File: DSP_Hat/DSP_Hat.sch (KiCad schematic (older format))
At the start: 27 parts, among them P1 Conn_02x20_Odd_Even

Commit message: more work on timing crytal
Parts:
- added C?: 0.1uF, symbol Device:C_Small
- added L?: L_Core_Ferrite, symbol Device:L_Core_Ferrite
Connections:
- wire segments 129 -> 139
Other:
- moved on the sheet: R?
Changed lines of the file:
@@
 U 1 1 5CABFE49
 P 10000 2900
-F 0 "X?" H 10000 2422 50  0000 C CNN
-F 1 "25MHz" H 10000 2513 50  0000 C CNN
+F 0 "X?" H 10250 2500 50  0000 R CNN
+F 1 "25MHz" H 10300 2600 50  0000 R CNN
 F 2 "Oscillator:Oscillator_SMD_Abracon_ASV-4Pin_7.0x5.1mm" H 10700 2550 50  0001 C CNN
 F 3 "http://www.abracon.com/Oscillators/ASV.pdf" H 9900 2900 50  0001 C CNN
@@
 Text Label 9000 2900 2    50   ~ 0
 MCLK
-Wire Wire Line
-	10000 3200 10000 3450
-Wire Wire Line
-	10000 3450 10600 3450
 $Comp
 L power:GND #PWR?
 U 1 1 5CADBC01
-P 10600 3450
-F 0 "#PWR?" H 10600 3200 50  0001 C CNN
-F 1 "GND" V 10605 3322 50  0000 R CNN
-F 2 "" H 10600 3450 50  0001 C CNN
-F 3 "" H 10600 3450 50  0001 C CNN
-	1    10600 3450
+P 10600 2400
+F 0 "#PWR?" H 10600 2150 50  0001 C CNN
+F 1 "GND" V 10605 2272 50  0000 R CNN
+F 2 "" H 10600 2400 50  0001 C CNN
+F 3 "" H 10600 2400 50  0001 C CNN
+	1    10600 2400
 	0    -1   -1   0
 $EndComp
@@
 L Device:R R?
 U 1 1 5CAE0FF9
-P 10500 2900
-F 0 "R?" V 10293 2900 50  0000 C CNN
-F 1 "10k" V 10384 2900 50  0000 C CNN
-F 2 "" V 10430 2900 50  0001 C CNN
-F 3 "~" H 10500 2900 50  0001 C CNN
-	1    10500 2900
+P 10600 2900
+F 0 "R?" V 10715 2900 50  0000 C CNN
+F 1 "10k" V 10806 2900 50  0000 C CNN
+F 2 "" V 10530 2900 50  0001 C CNN
+F 3 "~" H 10600 2900 50  0001 C CNN
+	1    10600 2900
+	0    1    1    0
+$EndComp
+Wire Wire Line
+	10750 2900 10800 2900
+Wire Wire Line
+	10300 2900 10450 2900
+Wire Wire Line
+	10000 2600 10000 2400
+Wire Wire Line
+	10000 2400 10350 2400
+Wire Wire Line
+	10000 3450 10250 3450
+$Comp
+L Device:L_Core_Ferrite L?
+U 1 1 5CA3E2B6
+P 10400 3450
+F 0 "L?" V 10532 3450 50  0000 C CNN
+F 1 "L_Core_Ferrite" V 10623 3450 50  0000 C CNN
+F 2 "" H 10400 3450 50  0001 C CNN
+F 3 "~" H 10400 3450 50  0001 C CNN
+	1    10400 3450
 	0    1    1    0
 $EndComp
 $Comp
-L power:GND #PWR?
-U 1 1 5CAE5CF4
-P 10800 2900
-F 0 "#PWR?" H 10800 2650 50  0001 C CNN
-F 1 "GND" V 10805 2772 50  0000 R CNN
-F 2 "" H 10800 2900 50  0001 C CNN
-F 3 "" H 10800 2900 50  0001 C CNN
-	1    10800 2900
-	0    -1   -1   0
+L power:+3.3V #PWR?
+U 1 1 5CA449F1
+P 10650 3450
+F 0 "#PWR?" H 10650 3300 50  0001 C CNN
+F 1 "+3.3V" V 10665 3578 50  0000 L CNN
+F 2 "" H 10650 3450 50  0001 C CNN
+F 3 "" H 10650 3450 50  0001 C CNN
+	1    10650 3450
+	0    1    1    0
 $EndComp
 Wire Wire Line
-	10650 2900 10800 2900
+	10550 3450 10650 3450
 Wire Wire Line
-	10300 2900 10350 2900
+	10000 3200 10000 3250
+$Comp
+L Device:C_Small C?
+U 1 1 5CA6F896
+P 10350 2650
+F 0 "C?" H 10442 2696 50  0000 L CNN
+F 1 "0.1uF" H 10442 2605 50  0000 L CNN
+F 2 "" H 10350 2650 50  0001 C CNN
+F 3 "~" H 10350 2650 50  0001 C CNN
+	1    10350 2650
+	1    0    0    -1
+$EndComp
+Wire Wire Line
+	10350 2550 10350 2400
+Connection ~ 10350 2400
+Wire Wire Line
+	10350 2400 10600 2400
+Wire Wire Line
+	10800 2900 10800 3250
+Wire Wire Line
+	10800 3250 10000 3250
+Connection ~ 10000 3250
+Wire Wire Line
+	10000 3250 10000 3450
+Wire Wire Line
+	10350 2750 10350 3200
+Wire Wire Line
+	10350 3200 10000 3200
+Connection ~ 10000 3200
 $EndSCHEMATC

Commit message: more work on schematic
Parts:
- removed R?: 49.9, symbol Device:R
- removed Y?: 25 MHz, symbol Device:Crystal
- gave numbers to parts that had none: 22
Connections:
- wire segments 139 -> 137

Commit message: farted around some more with DSP Hat
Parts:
- R2, R3, R4, R5: footprint (none) -> Resistor_SMD:R_0402_1005Metric
- U1: footprint CP_32_4 -> DSP_Hat:ADAU1761BCPZ-R7
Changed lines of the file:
@@
 F 0 "U1" H 5750 4587 60  0000 C CNN
 F 1 "ADAU1761BCPZ-R7" H 5750 4481 60  0000 C CNN
-F 2 "CP_32_4" H 5750 4440 60  0001 C CNN
+F 2 "DSP_Hat:ADAU1761BCPZ-R7" H 5750 4440 60  0001 C CNN
 F 3 "" H 3650 4200 60  0000 C CNN
 	1    3650 4200
@@
 F 0 "R2" H 6670 2096 50  0000 L CNN
 F 1 "2k" H 6670 2005 50  0000 L CNN
-F 2 "" V 6530 2050 50  0001 C CNN
+F 2 "Resistor_SMD:R_0402_1005Metric" V 6530 2050 50  0001 C CNN
 F 3 "~" H 6600 2050 50  0001 C CNN
 	1    6600 2050
@@
 F 0 "R3" H 6670 2496 50  0000 L CNN
 F 1 "2k" H 6670 2405 50  0000 L CNN
-F 2 "" V 6530 2450 50  0001 C CNN
+F 2 "Resistor_SMD:R_0402_1005Metric" V 6530 2450 50  0001 C CNN
 F 3 "~" H 6600 2450 50  0001 C CNN
 	1    6600 2450
@@
 F 0 "R4" V 9193 2900 50  0000 C CNN
 F 1 "49.9" V 9284 2900 50  0000 C CNN
-F 2 "" V 9330 2900 50  0001 C CNN
+F 2 "Resistor_SMD:R_0402_1005Metric" V 9330 2900 50  0001 C CNN
 F 3 "~" H 9400 2900 50  0001 C CNN
 	1    9400 2900
@@
 F 0 "R5" V 10715 2900 50  0000 C CNN
 F 1 "10k" V 10806 2900 50  0000 C CNN
-F 2 "" V 10530 2900 50  0001 C CNN
+F 2 "Resistor_SMD:R_0402_1005Metric" V 10530 2900 50  0001 C CNN
 F 3 "~" H 10600 2900 50  0001 C CNN
 	1    10600 2900

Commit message: placing more PCB footprints
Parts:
- added C13: 9.1 pF, Capacitor_SMD:C_0603_1608Metric_Pad1.05x0.95mm_HandSolder, symbol Device:C_Small
- C1, C2: footprint (none) -> Capacitor_SMD:C_0805_2012Metric_Pad1.15x1.40mm_HandSolder
- C3, C4, C5: footprint (none) -> Capacitor_SMD:C_0603_1608Metric_Pad1.05x0.95mm_HandSolder
- L2: footprint (none) -> Inductor_SMD:L_0402_1005Metric
- R4: footprint Resistor_SMD:R_0402_1005Metric -> Resistor_SMD:R_0603_1608Metric
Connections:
- wire segments 137 -> 138
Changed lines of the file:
@@
 F 0 "C2" H 1688 4446 50  0000 L CNN
 F 1 "10uF" H 1688 4355 50  0000 L CNN
-F 2 "" H 1600 4400 50  0001 C CNN
+F 2 "Capacitor_SMD:C_0805_2012Metric_Pad1.15x1.40mm_HandSolder" H 1600 4400 50  0001 C CNN
 F 3 "~" H 1600 4400 50  0001 C CNN
 	1    1600 4400
@@
 F 0 "C4" H 2092 4446 50  0000 L CNN
 F 1 "0.1uF" H 2092 4355 50  0000 L CNN
-F 2 "" H 2000 4400 50  0001 C CNN
+F 2 "Capacitor_SMD:C_0603_1608Metric_Pad1.05x0.95mm_HandSolder" H 2000 4400 50  0001 C CNN
 F 3 "~" H 2000 4400 50  0001 C CNN
 	1    2000 4400
@@
 	0    -1   -1   0
 $EndComp
-Wire Wire Line
-	3650 4900 2300 4900
 $Comp
 L power:+3.3V #PWR01
@@
 L power:GND #PWR07
 U 1 1 5CA96405
-P 2650 5400
-F 0 "#PWR07" H 2650 5150 50  0001 C CNN
-F 1 "GND" V 2655 5272 50  0000 R CNN
-F 2 "" H 2650 5400 50  0001 C CNN
-F 3 "" H 2650 5400 50  0001 C CNN
-	1    2650 5400
+P 2650 5650
+F 0 "#PWR07" H 2650 5400 50  0001 C CNN
+F 1 "GND" V 2655 5522 50  0000 R CNN
+F 2 "" H 2650 5650 50  0001 C CNN
+F 3 "" H 2650 5650 50  0001 C CNN
+	1    2650 5650
 	0    -1   -1   0
 $EndComp
@@
 F 0 "C1" H 1238 5196 50  0000 L CNN
 F 1 "10uF" H 1238 5105 50  0000 L CNN
-F 2 "" H 1150 5150 50  0001 C CNN
+F 2 "Capacitor_SMD:C_0805_2012Metric_Pad1.15x1.40mm_HandSolder" H 1150 5150 50  0001 C CNN
 F 3 "~" H 1150 5150 50  0001 C CNN
 	1    1150 5150
@@
 F 0 "C3" H 1692 5196 50  0000 L CNN
 F 1 "0.1uF" H 1692 5105 50  0000 L CNN
-F 2 "" H 1600 5150 50  0001 C CNN
+F 2 "Capacitor_SMD:C_0603_1608Metric_Pad1.05x0.95mm_HandSolder" H 1600 5150 50  0001 C CNN
 F 3 "~" H 1600 5150 50  0001 C CNN
 	1    1600 5150
@@
 F 0 "C5" H 2142 5196 50  0000 L CNN
 F 1 "0.1uF" H 2142 5105 50  0000 L CNN
-F 2 "" H 2050 5150 50  0001 C CNN
+F 2 "Capacitor_SMD:C_0603_1608Metric_Pad1.05x0.95mm_HandSolder" H 2050 5150 50  0001 C CNN
 F 3 "~" H 2050 5150 50  0001 C CNN
 	1    2050 5150
 	-1   0    0    -1
 $EndComp
-$Comp
-L pspice:INDUCTOR L1
-U 1 1 5CA96686
-P 2300 5150
-F 0 "L1" V 2254 5228 50  0000 L CNN
-F 1 "1.2nH" V 2345 5228 50  0000 L CNN
-F 2 "" H 2300 5150 50  0001 C CNN
-F 3 "~" H 2300 5150 50  0001 C CNN
-	1    2300 5150
-	0    1    1    0
-$EndComp
-Connection ~ 2300 4900
 Wire Wire Line
 	1150 4900 1150 5050
@@
 	2050 4900 2300 4900
 Wire Wire Line
-	1150 5250 1150 5400
-Wire Wire Line
-	1150 5400 1600 5400
-Connection ~ 2300 5400
-Wire Wire Line
-	2300 5400 2650 5400
-Wire Wire Line
-	1600 5250 1600 5400
-Connection ~ 1600 5400
-Wire Wire Line
-	1600 5400 2050 5400
-Wire Wire Line
-	2050 5250 2050 5400
-Connection ~ 2050 5400
-Wire Wire Line
-	2050 5400 2300 5400
+	1150 5250 1150 5650
+Wire Wire Line
+	1150 5650 1600 5650
+Wire Wire Line
+	2050 5250 2050 5650
 Wire Wire Line
 	3500 4300 3650 4300
@@
 F 0 "R4" V 9193 2900 50  0000 C CNN
 F 1 "49.9" V 9284 2900 50  0000 C CNN
-F 2 "Resistor_SMD:R_0402_1005Metric" V 9330 2900 50  0001 C CNN
+F 2 "Resistor_SMD:R_0603_1608Metric" V 9330 2900 50  0001 C CNN
 F 3 "~" H 9400 2900 50  0001 C CNN
 	1    9400 2900
@@
 F 0 "L2" V 10532 3450 50  0000 C CNN
 F 1 "L_Core_Ferrite" V 10623 3450 50  0000 C CNN
-F 2 "" H 10400 3450 50  0001 C CNN
+F 2 "Inductor_SMD:L_0402_1005Metric" H 10400 3450 50  0001 C CNN
 F 3 "~" H 10400 3450 50  0001 C CNN
 	1    10400 3450
@@
 Text Label 3500 4300 2    50   ~ 0
 MCLK
+$Comp
+L pspice:INDUCTOR L1
+U 1 1 5CA96686
+P 2300 5200
+F 0 "L1" V 2254 5278 50  0000 L CNN
+F 1 "1.2nH" V 2345 5278 50  0000 L CNN
+F 2 "" H 2300 5200 50  0001 C CNN
+F 3 "~" H 2300 5200 50  0001 C CNN
+	1    2300 5200
+	0    1    1    0
+$EndComp
+Connection ~ 2300 4900
+Wire Wire Line
+	2300 4900 3650 4900
+Wire Wire Line
+	2050 5650 2300 5650
+Connection ~ 2050 5650
+Wire Wire Line
+	1600 5250 1600 5650
+Connection ~ 1600 5650
+Wire Wire Line
+	1600 5650 2050 5650
+$Comp
+L Device:C_Small C13
+U 1 1 5CAE5AF1
+P 2300 5550
+F 0 "C13" H 2208 5596 50  0000 R CNN
+F 1 "9.1 pF" H 2208 5505 50  0000 R CNN
+F 2 "Capacitor_SMD:C_0603_1608Metric_Pad1.05x0.95mm_HandSolder" H 2300 5550 50  0001 C CNN
+F 3 "~" H 2300 5550 50  0001 C CNN
+	1    2300 5550
+	-1   0    0    -1
+$EndComp
+Connection ~ 2300 5650
+Wire Wire Line
+	2300 5650 2650 5650
+Wire Wire Line
+	2300 4950 2300 4900
 $EndSCHEMATC

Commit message: overhaul of schematic
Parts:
- removed C1, C2: 10uF, Capacitor_SMD:C_0805_2012Metric_Pad1.15x1.40mm_HandSolder, symbol Device:CP_Small
- removed C10, C11: 0.1uF, symbol Device:C_Small
- removed C12: 10uF, symbol Device:CP_Small
- removed C13: 9.1 pF, Capacitor_SMD:C_0603_1608Metric_Pad1.05x0.95mm_HandSolder, symbol Device:C_Small
- removed C3, C4, C5: 0.1uF, Capacitor_SMD:C_0603_1608Metric_Pad1.05x0.95mm_HandSolder, symbol Device:C_Small
- removed C6, C7, C8, C9: 10uf, symbol Device:C
- removed L1: 1.2nH, symbol pspice:INDUCTOR
- removed L2: L_Core_Ferrite, Inductor_SMD:L_0402_1005Metric, symbol Device:L_Core_Ferrite
- removed MK5: Left Microphone, symbol Device:Microphone
- removed MK6: Right Microphone, symbol Device:Microphone
- removed R2, R3: 2k, Resistor_SMD:R_0402_1005Metric, symbol Device:R
- removed R4: 49.9, Resistor_SMD:R_0603_1608Metric, symbol Device:R
- removed R5: 10k, Resistor_SMD:R_0402_1005Metric, symbol Device:R
- removed U1: ADAU1761BCPZ-R7, DSP_Hat:ADAU1761BCPZ-R7, symbol 2019-03-30_11-52-36:ADAU1761BCPZ-R7
- removed X1: 25MHz, Oscillator:Oscillator_SMD_Abracon_ASV-4Pin_7.0x5.1mm, symbol Oscillator:ASV-xxxMHz
- added C? (x11): CAP, symbol pspice:CAP
- added J?: AudioJack2_Ground_Switch, symbol Connector:AudioJack2_Ground_Switch
- added L?: L_Core_Ferrite, symbol Device:L_Core_Ferrite
- added R? (x6): R, symbol Device:R
- added U?: ADAU1761BCPZ-R7_2, CP_32_4, symbol 2019-03-30_11-52-36:ADAU1761BCPZ-R7_2
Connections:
- net labels added: ADAIU761_ADDR0, ADAIU761_ADDR1, ADC_SDATA, BCLK, DAC_SDATA, LEFT_LOOP, LOUTN, LOUTP, LRCLK, RIGHT_LOOP, ROUTN, ROUTP, TWI0_SCL, TWIO_SDA
- net labels removed: LINN, LINP, MCLK, MICBIAS, RINN, RINP
- wire segments 138 -> 145

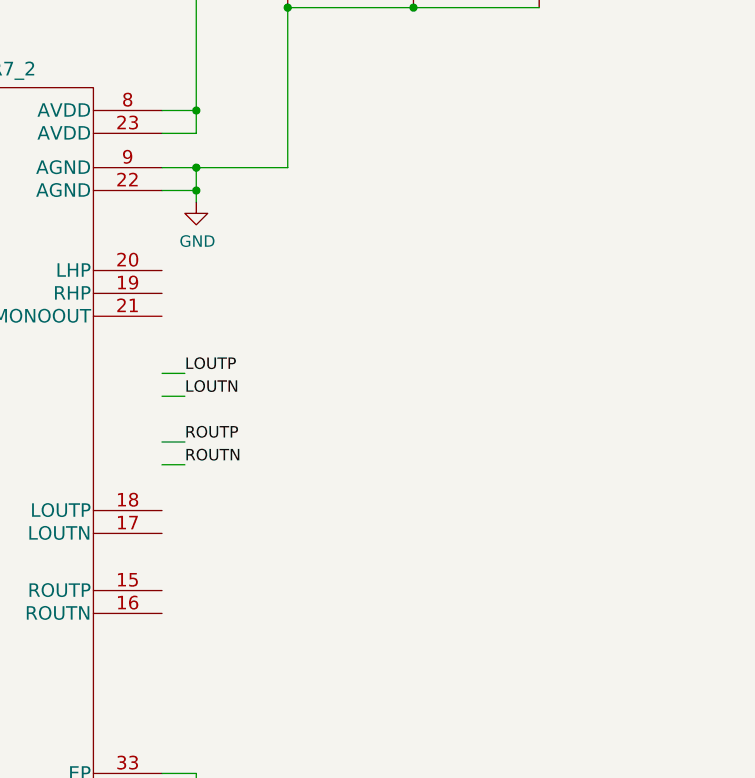
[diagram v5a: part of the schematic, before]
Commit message: edits to symbol for ADAU1761
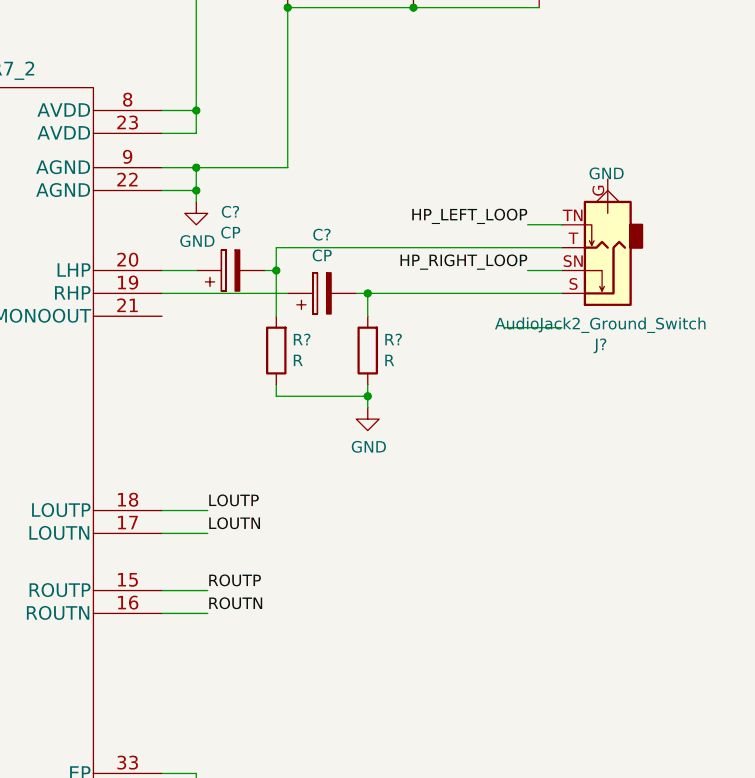
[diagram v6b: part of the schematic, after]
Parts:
- added C? (x2): CP, symbol Device:CP
- added J?: AudioJack2_Ground_Switch, symbol Connector:AudioJack2_Ground_Switch
- added R? (x2): R, symbol Device:R
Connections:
- net labels added: HP_LEFT_LOOP, HP_RIGHT_LOOP
- wire segments 145 -> 161
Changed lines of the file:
@@
 	6050 6500 6550 6500
 Connection ~ 6550 6500
-Wire Wire Line
-	8800 4050 8900 4050
-Wire Wire Line
-	8800 4150 8900 4150
-Wire Wire Line
-	8800 4350 8900 4350
-Wire Wire Line
-	8800 4450 8900 4450
-Text Label 8900 4050 0    50   ~ 0
-LOUTP
-Text Label 8900 4150 0    50   ~ 0
-LOUTN
-Text Label 8900 4350 0    50   ~ 0
-ROUTP
-Text Label 8900 4450 0    50   ~ 0
-ROUTN
 $Comp
 L power:GND #PWR?
@@
 	1    0    0    -1
 $EndComp
+$Comp
+L Connector:AudioJack2_Ground_Switch J?
+U 1 1 5CCA20D9
+P 10750 3500
+F 0 "J?" H 10780 3925 50  0000 C CNN
+F 1 "AudioJack2_Ground_Switch" H 10780 3834 50  0000 C CNN
+F 2 "" H 10750 3700 50  0001 C CNN
+F 3 "~" H 10750 3700 50  0001 C CNN
+	1    10750 3500
+	-1   0    0    1
+$EndComp
+$Comp
+L power:GND #PWR?
+U 1 1 5CCA2325
+P 10750 3350
+F 0 "#PWR?" H 10750 3100 50  0001 C CNN
+F 1 "GND" H 10755 3177 50  0000 C CNN
+F 2 "" H 10750 3350 50  0001 C CNN
+F 3 "" H 10750 3350 50  0001 C CNN
+	1    10750 3350
+	-1   0    0    1
+$EndComp
+$Comp
+L Device:CP C?
+U 1 1 5CCA2D40
+P 9100 3600
+F 0 "C?" V 9355 3600 50  0000 C CNN
+F 1 "CP" V 9264 3600 50  0000 C CNN
+F 2 "" H 9138 3450 50  0001 C CNN
+F 3 "~" H 9100 3600 50  0001 C CNN
+	1    9100 3600
+	0    -1   -1   0
+$EndComp
+Wire Wire Line
+	8800 3600 8950 3600
+Wire Wire Line
+	10300 3850 10550 3850
+$Comp
+L Device:CP C?
+U 1 1 5CCCE97F
+P 9500 3700
+F 0 "C?" V 9755 3700 50  0000 C CNN
+F 1 "CP" V 9664 3700 50  0000 C CNN
+F 2 "" H 9538 3550 50  0001 C CNN
+F 3 "~" H 9500 3700 50  0001 C CNN
+	1    9500 3700
+	0    -1   -1   0
+$EndComp
+Wire Wire Line
+	8800 3700 9350 3700
+Wire Wire Line
+	9300 3500 10550 3500
+Wire Wire Line
+	10550 3400 10400 3400
+Wire Wire Line
+	10550 3600 10400 3600
+Text Label 10400 3400 2    50   ~ 0
+HP_LEFT_LOOP
+Text Label 10400 3600 2    50   ~ 0
+HP_RIGHT_LOOP
+$Comp
+L power:GND #PWR?
+U 1 1 5CCF5B0C
+P 9700 4200
+F 0 "#PWR?" H 9700 3950 50  0001 C CNN
+F 1 "GND" H 9705 4027 50  0000 C CNN
+F 2 "" H 9700 4200 50  0001 C CNN
+F 3 "" H 9700 4200 50  0001 C CNN
+	1    9700 4200
+	1    0    0    -1
+$EndComp
+$Comp
+L Device:R R?
+U 1 1 5CCF5BDB
+P 9700 3950
+F 0 "R?" H 9630 3904 50  0000 R CNN
+F 1 "R" H 9630 3995 50  0000 R CNN
+F 2 "" V 9630 3950 50  0001 C CNN
+F 3 "~" H 9700 3950 50  0001 C CNN
+	1    9700 3950
+	-1   0    0    1
+$EndComp
+$Comp
+L Device:R R?
+U 1 1 5CCF5E35
+P 9300 3950
+F 0 "R?" H 9230 3904 50  0000 R CNN
+F 1 "R" H 9230 3995 50  0000 R CNN
+F 2 "" V 9230 3950 50  0001 C CNN
+F 3 "~" H 9300 3950 50  0001 C CNN
+	1    9300 3950
+	-1   0    0    1
+$EndComp
+Wire Wire Line
+	9700 4100 9700 4150
+Wire Wire Line
+	9700 3800 9700 3700
+Wire Wire Line
+	9700 3700 10550 3700
+Wire Wire Line
+	9300 4100 9300 4150
+Wire Wire Line
+	9300 4150 9700 4150
+Connection ~ 9700 4150
+Wire Wire Line
+	9700 4150 9700 4200
+Wire Wire Line
+	9300 3800 9300 3600
+Wire Wire Line
+	9250 3600 9300 3600
+Connection ~ 9300 3600
+Wire Wire Line
+	9300 3600 9300 3500
+Wire Wire Line
+	9650 3700 9700 3700
+Connection ~ 9700 3700
+Wire Wire Line
+	8800 5100 9000 5100
+Wire Wire Line
+	8800 5000 9000 5000
+Wire Wire Line
+	8800 4750 9000 4750
+Wire Wire Line
+	8800 4650 9000 4650
+Text Label 9000 4650 0    50   ~ 0
+LOUTP
+Text Label 9000 4750 0    50   ~ 0
+LOUTN
+Text Label 9000 5000 0    50   ~ 0
+ROUTP
+Text Label 9000 5100 0    50   ~ 0
+ROUTN
 $EndSCHEMATC

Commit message: what are your values?
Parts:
- removed C? (x11): CAP, symbol pspice:CAP
- added C? (x6): 10uF, symbol Device:C_Small
- added C? (x3): 0.1uF, symbol Device:C_Small
- added C? (x2): 0.1 uF, symbol Device:C_Small
- C? (x2): value CP -> 100uF
- FER?: renamed from L?; value L_Core_Ferrite -> 600
- R? (x4): value R -> 100K
- R? (x2): value R -> 470.0K
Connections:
- net +3V3: now also C?.1, C?.1; no longer U?.24 (DVDDOUT)
- net GND: now also C?.1, C?.1, C?.2, C?.2, C?.2, C?.2, C?.2, C?.2, C?.2
- net at U?.10 (LINP), U?.12 (RINP), U?.14 (RAUX)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: now also C?.2, C?.2
- net at R?.2, U?.11 (LINN): now also C?.1
- net at R?.2, U?.13 (RINN): now also C?.1
- net at FER?.1, U?.23 (AVDD), U?.8 (AVDD): now also C?.1, C?.1, C?.1
- net at J?.S, R?.2: now also C?.2
- net at J?.T, R?.2: now also C?.2
- new net: C?.1, C?.1, U?.24 (DVDDOUT)
- no-connect marks 0 -> 1
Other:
- moved on the sheet: FER?

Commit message: added osc
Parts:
- added R? (x2): R, symbol Device:R
- added R? (x2): 10K, symbol Device:R
- added Y?: ASFLMB-12.288MHZ-LC-T_0, ASFLMB_Series, symbol 2019-04-10_00-18-11:ASFLMB-12.288MHZ-LC-T_0
- R?: value R -> 33
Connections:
- net +3V3: now also Y?.4 (VDD)
- net GND: now also R?.2, Y?.2 (GND)
- net HP_LEFT_LOOP: now also R?.1
- net HP_RIGHT_LOOP: now also R?.1
- net LEFT_LOOP: now also R?.2
- net RIGHT_LOOP: now also R?.2
- net at R?.1: now also Y?.3 (OUTPUT)
- new net: R?.1, R?.2, Y?.1 (STBY)
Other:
- moved on the sheet: R?
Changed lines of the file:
@@
 	4150 4050 5000 4050
 Connection ~ 5000 4050
-Wire Wire Line
-	6850 5800 6800 5800
-Connection ~ 6800 5800
-Wire Wire Line
-	6800 5800 3700 5800
 $Comp
 L Device:R R?
 U 1 1 5CC86ACB
-P 3550 5800
-F 0 "R?" V 3757 5800 50  0000 C CNN
-F 1 "R" V 3666 5800 50  0000 C CNN
-F 2 "" V 3480 5800 50  0001 C CNN
-F 3 "~" H 3550 5800 50  0001 C CNN
-	1    3550 5800
+P 5250 5800
+F 0 "R?" V 5457 5800 50  0000 C CNN
+F 1 "33" V 5366 5800 50  0000 C CNN
+F 2 "" V 5180 5800 50  0001 C CNN
+F 3 "~" H 5250 5800 50  0001 C CNN
+	1    5250 5800
 	0    -1   -1   0
 $EndComp
@@
 	6550 6400 6550 6300
 Connection ~ 6550 6400
+$Comp
+L Device:R R?
+U 1 1 5CAE0EC7
+P 10150 5700
+F 0 "R?" V 9943 5700 50  0000 C CNN
+F 1 "R" V 10034 5700 50  0000 C CNN
+F 2 "" V 10080 5700 50  0001 C CNN
+F 3 "~" H 10150 5700 50  0001 C CNN
+	1    10150 5700
+	0    1    1    0
+$EndComp
+$Comp
+L Device:R R?
+U 1 1 5CAE0FB9
+P 10150 5900
+F 0 "R?" V 10265 5900 50  0000 C CNN
+F 1 "R" V 10356 5900 50  0000 C CNN
+F 2 "" V 10080 5900 50  0001 C CNN
+F 3 "~" H 10150 5900 50  0001 C CNN
+	1    10150 5900
+	0    1    1    0
+$EndComp
+Wire Wire Line
+	10300 5700 10400 5700
+Text Label 10400 5700 0    50   ~ 0
+HP_LEFT_LOOP
+Text Label 10400 5900 0    50   ~ 0
+HP_RIGHT_LOOP
+Wire Wire Line
+	10300 5900 10400 5900
+Wire Wire Line
+	10000 5700 9900 5700
+Wire Wire Line
+	10000 5900 9900 5900
+Text Label 9900 5700 2    50   ~ 0
+LEFT_LOOP
+Text Label 9900 5900 2    50   ~ 0
+RIGHT_LOOP
+$Comp
+L 2019-04-10_00-18-11:ASFLMB-12.288MHZ-LC-T_0 Y?
+U 1 1 5CAFC494
+P 2500 5700
+F 0 "Y?" H 3175 6087 60  0000 C CNN
+F 1 "ASFLMB-12.288MHZ-LC-T_0" H 3175 5981 60  0000 C CNN
+F 2 "ASFLMB_Series" H 3150 5950 60  0001 C CNN
+F 3 "" H 2500 5700 60  0000 C CNN
+	1    2500 5700
+	1    0    0    -1
+$EndComp
+Wire Wire Line
+	6800 5800 5400 5800
+Wire Wire Line
+	3850 5800 5100 5800
+$Comp
+L power:+3.3V #PWR?
+U 1 1 5CB3DF76
+P 4100 5700
+F 0 "#PWR?" H 4100 5550 50  0001 C CNN
+F 1 "+3.3V" V 4115 5828 50  0000 L CNN
+F 2 "" H 4100 5700 50  0001 C CNN
+F 3 "" H 4100 5700 50  0001 C CNN
+	1    4100 5700
+	0    1    1    0
+$EndComp
+Wire Wire Line
+	3850 5700 4100 5700
+$Comp
+L power:GND #PWR?
+U 1 1 5CB462D9
+P 2350 5800
+F 0 "#PWR?" H 2350 5550 50  0001 C CNN
+F 1 "GND" V 2355 5672 50  0000 R CNN
+F 2 "" H 2350 5800 50  0001 C CNN
+F 3 "" H 2350 5800 50  0001 C CNN
+	1    2350 5800
+	0    1    1    0
+$EndComp
+Wire Wire Line
+	2350 5800 2500 5800
+Wire Wire Line
+	2500 5700 1900 5700
+$Comp
+L power:GND #PWR?
+U 1 1 5CB5FE44
+P 1900 6100
+F 0 "#PWR?" H 1900 5850 50  0001 C CNN
+F 1 "GND" H 1905 5927 50  0000 C CNN
+F 2 "" H 1900 6100 50  0001 C CNN
+F 3 "" H 1900 6100 50  0001 C CNN
+	1    1900 6100
+	1    0    0    -1
+$EndComp
+$Comp
+L power:+3.3V #PWR?
+U 1 1 5CB5FED0
+P 1900 5300
+F 0 "#PWR?" H 1900 5150 50  0001 C CNN
+F 1 "+3.3V" H 1915 5473 50  0000 C CNN
+F 2 "" H 1900 5300 50  0001 C CNN
+F 3 "" H 1900 5300 50  0001 C CNN
+	1    1900 5300
+	1    0    0    -1
+$EndComp
+$Comp
+L Device:R R?
+U 1 1 5CB5FF6A
+P 1900 5500
+F 0 "R?" H 1970 5546 50  0000 L CNN
+F 1 "10K" H 1970 5455 50  0000 L CNN
+F 2 "" V 1830 5500 50  0001 C CNN
+F 3 "~" H 1900 5500 50  0001 C CNN
+	1    1900 5500
+	1    0    0    -1
+$EndComp
+$Comp
+L Device:R R?
+U 1 1 5CB6005E
+P 1900 5900
+F 0 "R?" H 1970 5946 50  0000 L CNN
+F 1 "10K" H 1970 5855 50  0000 L CNN
+F 2 "" V 1830 5900 50  0001 C CNN
+F 3 "~" H 1900 5900 50  0001 C CNN
+	1    1900 5900
+	1    0    0    -1
+$EndComp
+Wire Wire Line
+	1900 5700 1900 5650
+Wire Wire Line
+	1900 5700 1900 5750
+Connection ~ 1900 5700
+Wire Wire Line
+	1900 6050 1900 6100
 $EndSCHEMATC
